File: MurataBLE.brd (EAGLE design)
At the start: 50 x 31 mm, 33 parts, among them IC1 IC_LDO_XX1117, IC3 74LVC1G00DBV, Q2 12MHz, SW1 SW_TACTSW_2PP8073, SW2 SW_TACTSW_2PP8073, SW3 SW_TACTSW_2PP8073, U1 IC_BLE_LBCA2HNZYZ-711, X1 TSW-112-02-S-S

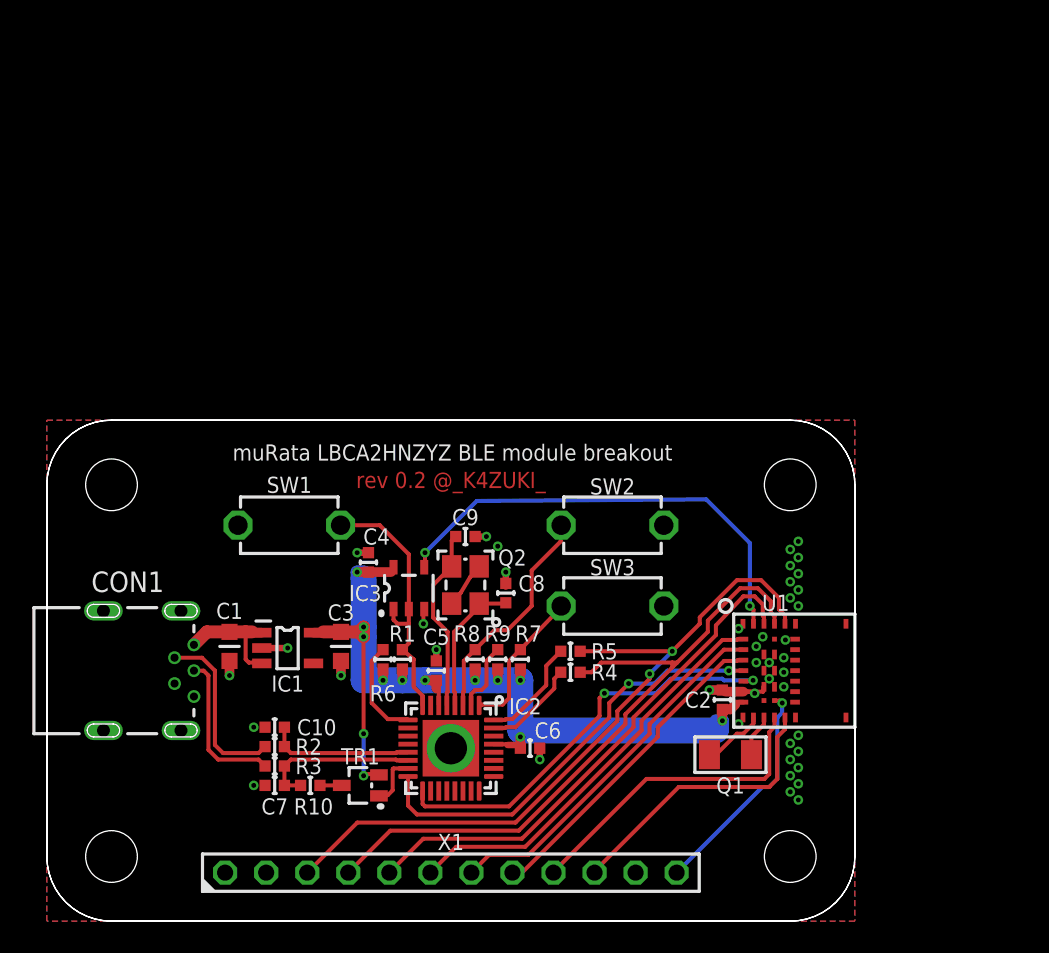
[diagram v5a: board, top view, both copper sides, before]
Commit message: [ USB ][ FIX ] Dimention; PMOS replace; silk on pinheader; via - demention changed to 60x55mm, vcut and milling added - PMOS replaced as schematic update - silk added on X1 pin header - via slight move - related trace change
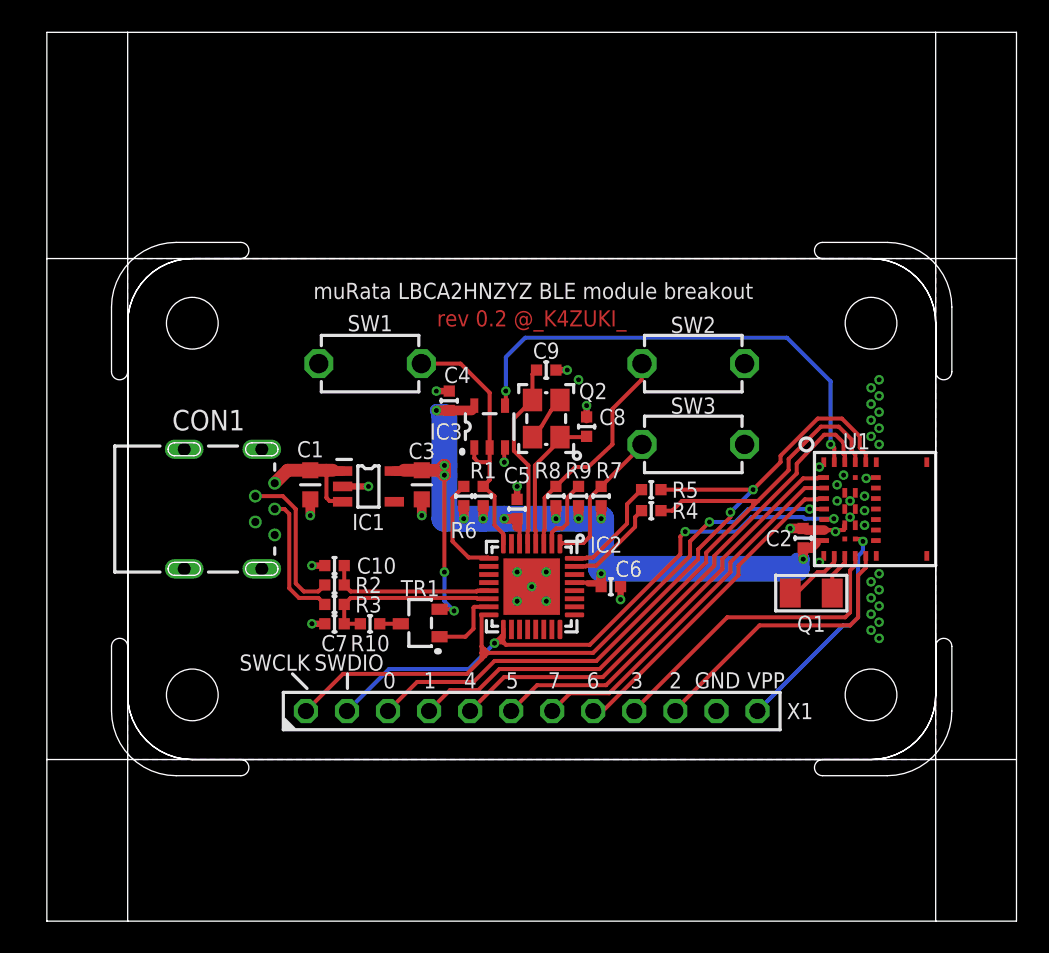
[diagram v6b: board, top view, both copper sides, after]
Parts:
- C1, C3: value (none) -> 1u/1608
- C2, C4, C5, C6: value (none) -> 0.1u/1005
- R1, R6, R7, R8, R9: value (none) -> 10k/1005
- R10: value (none) -> 1.5k/1005
- R2, R3: value (none) -> 33/1005
- R4, R5: value (none) -> 0R/1005
- SW1, SW2, SW3: value SW_TACTSW_2PP8073 -> P8073
- TR1: value NTS4173P -> I-4269; device mylib:SOT65P220X135-3N -> mylib:SOT95P300X140-3N
- moved C8 11.4 mm to (33.4, 30.6)
- moved C9 11.4 mm to (30.9, 34.1)
- moved Q2 11.4 mm to (30.9, 31.1)
- moved R1 11.3 mm to (27.0, 26.3)
- moved R6 11.3 mm to (25.8, 26.3)
- moved R8 11.3 mm to (31.5, 26.3)
- moved R9 11.3 mm to (32.9, 26.3)
- moved R7 11.3 mm to (34.3, 26.3)
- moved C4 11.2 mm to (24.9, 32.2)
- moved C1 11.2 mm to (16.3, 27.0)
- moved C2 11.2 mm to (46.8, 23.7)
- moved C3 11.2 mm to (23.2, 27.0)
- moved C5 11.2 mm to (29.1, 25.5)
- moved C6 11.2 mm to (34.9, 20.7)
- moved CON1 11.2 mm to (14.1, 25.5)
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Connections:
- net SWCLK: now also X1.1
- net SWDIO: now also X1.2
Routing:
- net SWCLK: track 27.0 -> 42.3 mm
- net SWDIO: track 25.9 -> 38.6 mm, vias 2 -> 3
- net GND: track 15.0 -> 26.2 mm, vias 44 -> 48
- net N$7: track 3.27 -> 4.58 mm
- net N$24: track 9.04 -> 10.3 mm
- net N$20: track 10.0 -> 11.3 mm
- net N$21: track 9.54 -> 8.24 mm
- net N$22: track 10.9 -> 9.60 mm
- net RESET: track 28.6 -> 29.9 mm
- net 3.3V: track 61.6 -> 62.4 mm
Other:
- board size 50 x 31 mm -> 60 x 55 mm
- board text added: "0"
- board text added: "1"
- board text added: "2"
- board text added: "3"
- board text added: "4"
- board text added: "5"
- board text added: "6"
- board text added: "7"
- board text added: "GND"
- board text added: "SWCLK"
- board text added: "SWDIO"
- board text added: "VPP"

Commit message: [ USB ][ FIX ] library update
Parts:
- CON1: value (none) -> C-2235
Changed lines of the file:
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@@
 <attribute name="VALUE" x="25.4" y="23.2" size="1.27" layer="27" ratio="16" rot="R270"/>
 </element>
-<element name="CON1" library="mylib" package="CON_USB_MINIB_AKI" value="" x="14.1" y="25.5" smashed="yes">
+<element name="CON1" library="mylib" package="CON_USB_MINIB_AKI" value="C-2235" x="14.1" y="25.5" smashed="yes">
 <attribute name="NAME" x="10" y="31" size="1.27" layer="25" font="vector" ratio="16" align="center"/>
 <attribute name="VALUE" x="7.8" y="19.2" size="1.27" layer="27" font="vector" ratio="16"/>

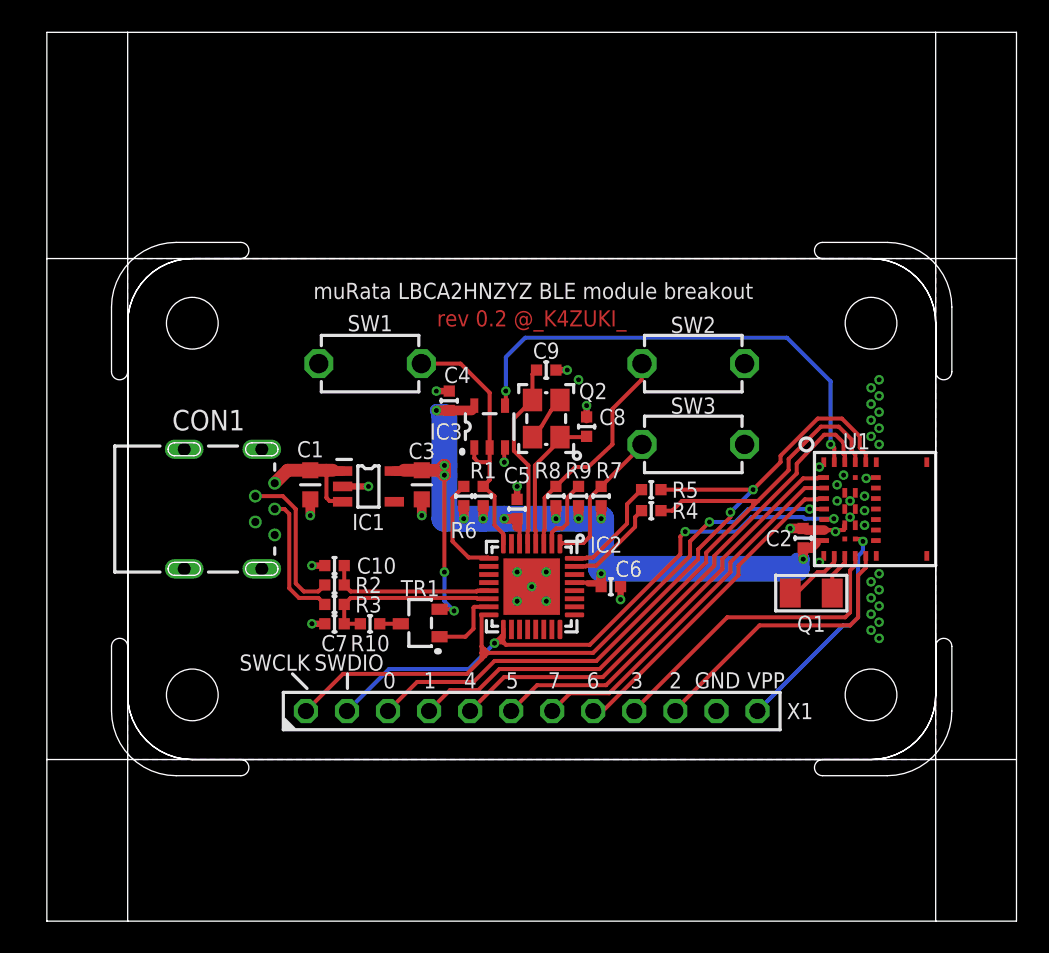
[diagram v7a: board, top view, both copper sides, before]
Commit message: [ USB ] moved 2mm north; bigger milling; add silk
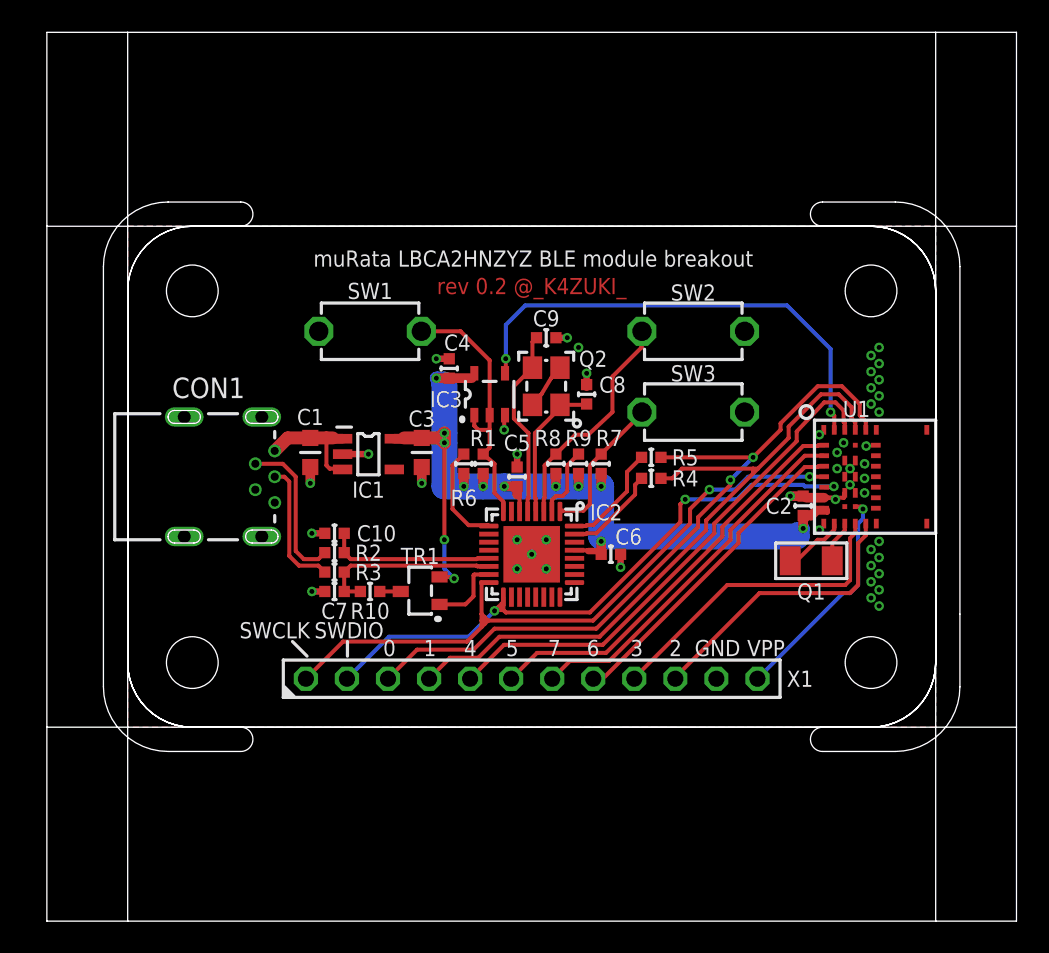
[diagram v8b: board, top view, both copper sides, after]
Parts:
- moved C1 2.00 mm to (16.3, 29.0)
- moved C10 2.00 mm to (17.8, 24.0)
- moved C2 2.00 mm to (46.8, 25.7)
- moved C3 2.00 mm to (23.2, 29.0)
- moved C4 2.00 mm to (24.9, 34.2)
- moved C5 2.00 mm to (29.1, 27.5)
- moved C6 2.00 mm to (34.9, 22.7)
- moved C7 2.00 mm to (17.8, 20.4)
- moved C8 2.00 mm to (33.4, 32.6)
- moved C9 2.00 mm to (30.9, 36.1)
- moved CON1 2.00 mm to (14.1, 27.5)
- moved IC1 2.00 mm to (19.9, 28.9)
- moved IC2 2.00 mm to (30.0, 22.7)
- moved IC3 2.00 mm to (27.4, 32.6)
- moved PCB1 2.00 mm to (30.0, 27.5)
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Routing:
- net 3.3V: track 62.4 -> 64.1 mm
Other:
- outline, holes or cut-outs redrawn
